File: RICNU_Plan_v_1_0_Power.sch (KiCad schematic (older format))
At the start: 15 parts, among them U1 TPS2113, U2 TLV62568

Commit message: Various small changes like comment removal
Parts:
- R1: value 20k -> 24k
- R5: value 450k -> 453k
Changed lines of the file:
@@
 P 8300 3900
 F 0 "R5" V 8400 3900 50  0000 C CNN
-F 1 "450k" V 8200 3900 50  0000 C CNN
+F 1 "453k" V 8200 3900 50  0000 C CNN
 F 2 "Resistors_SMD:R_0402_NoSilk" V 8230 3900 50  0001 C CNN
 F 3 "" H 8300 3900 50  0001 C CNN
@@
 P 3250 4150
 F 0 "R1" V 3300 3950 50  0000 C CNN
-F 1 "20k" V 3250 4150 50  0000 C CNN
+F 1 "24k" V 3250 4150 50  0000 C CNN
 F 2 "Resistors_SMD:R_0402_NoSilk" V 3180 4150 50  0001 C CNN
 F 3 "" H 3250 4150 50  0001 C CNN
@@
 L PWR_FLAG #FLG06
 U 1 1 5A03C349
-P 4900 5050
-F 0 "#FLG06" H 4900 5125 50  0001 C CNN
-F 1 "PWR_FLAG" H 4900 5200 50  0000 C CNN
-F 2 "" H 4900 5050 50  0001 C CNN
-F 3 "" H 4900 5050 50  0001 C CNN
-	1    4900 5050
+P 4900 5850
+F 0 "#FLG06" H 4900 5925 50  0001 C CNN
+F 1 "PWR_FLAG" H 4900 6000 50  0000 C CNN
+F 2 "" H 4900 5850 50  0001 C CNN
+F 3 "" H 4900 5850 50  0001 C CNN
+	1    4900 5850
 	-1   0    0    1
 $EndComp
@@
 L PWR_FLAG #FLG07
 U 1 1 5A03C34F
-P 4450 4950
-F 0 "#FLG07" H 4450 5025 50  0001 C CNN
-F 1 "PWR_FLAG" H 4450 5100 50  0000 C CNN
-F 2 "" H 4450 4950 50  0001 C CNN
-F 3 "" H 4450 4950 50  0001 C CNN
-	1    4450 4950
+P 4450 5750
+F 0 "#FLG07" H 4450 5825 50  0001 C CNN
+F 1 "PWR_FLAG" H 4450 5900 50  0000 C CNN
+F 2 "" H 4450 5750 50  0001 C CNN
+F 3 "" H 4450 5750 50  0001 C CNN
+	1    4450 5750
 	1    0    0    -1
 $EndComp
@@
 L GND #PWR08
 U 1 1 5A03C355
-P 4450 5050
-F 0 "#PWR08" H 4450 4800 50  0001 C CNN
-F 1 "GND" H 4450 4900 50  0000 C CNN
-F 2 "" H 4450 5050 50  0001 C CNN
-F 3 "" H 4450 5050 50  0001 C CNN
-	1    4450 5050
+P 4450 5850
+F 0 "#PWR08" H 4450 5600 50  0001 C CNN
+F 1 "GND" H 4450 5700 50  0000 C CNN
+F 2 "" H 4450 5850 50  0001 C CNN
+F 3 "" H 4450 5850 50  0001 C CNN
+	1    4450 5850
 	1    0    0    -1
 $EndComp
@@
 L +3V3 #PWR09
 U 1 1 5A03C35B
-P 4900 4950
-F 0 "#PWR09" H 4900 4800 50  0001 C CNN
-F 1 "+3V3" H 4900 5090 50  0000 C CNN
-F 2 "" H 4900 4950 50  0001 C CNN
-F 3 "" H 4900 4950 50  0001 C CNN
-	1    4900 4950
+P 4900 5750
+F 0 "#PWR09" H 4900 5600 50  0001 C CNN
+F 1 "+3V3" H 4900 5890 50  0000 C CNN
+F 2 "" H 4900 5750 50  0001 C CNN
+F 3 "" H 4900 5750 50  0001 C CNN
+	1    4900 5750
 	1    0    0    -1
 $EndComp
@@
 L +5V_USB #PWR010
 U 1 1 5A03C361
-P 5800 4950
-F 0 "#PWR010" H 5800 4800 50  0001 C CNN
-F 1 "+5V_USB" H 5800 5100 50  0000 C CNN
-F 2 "" H 5800 4950 50  0001 C CNN
-F 3 "" H 5800 4950 50  0001 C CNN
-	1    5800 4950
+P 5800 5750
+F 0 "#PWR010" H 5800 5600 50  0001 C CNN
+F 1 "+5V_USB" H 5800 5900 50  0000 C CNN
+F 2 "" H 5800 5750 50  0001 C CNN
+F 3 "" H 5800 5750 50  0001 C CNN
+	1    5800 5750
 	1    0    0    -1
 $EndComp
@@
 L PWR_FLAG #FLG011
 U 1 1 5A03C367
-P 5800 5050
-F 0 "#FLG011" H 5800 5125 50  0001 C CNN
-F 1 "PWR_FLAG" H 5800 5200 50  0000 C CNN
-F 2 "" H 5800 5050 50  0001 C CNN
-F 3 "" H 5800 5050 50  0001 C CNN
-	1    5800 5050
+P 5800 5850
+F 0 "#FLG011" H 5800 5925 50  0001 C CNN
+F 1 "PWR_FLAG" H 5800 6000 50  0000 C CNN
+F 2 "" H 5800 5850 50  0001 C CNN
+F 3 "" H 5800 5850 50  0001 C CNN
+	1    5800 5850
 	-1   0    0    1
 $EndComp
@@
 L +5V_USB_P #PWR012
 U 1 1 5A03C36D
-P 6250 4950
-F 0 "#PWR012" H 6250 4800 50  0001 C CNN
-F 1 "+5V_USB_P" H 6250 5100 50  0000 C CNN
-F 2 "" H 6250 4950 50  0001 C CNN
-F 3 "" H 6250 4950 50  0001 C CNN
-	1    6250 4950
+P 6250 5750
+F 0 "#PWR012" H 6250 5600 50  0001 C CNN
+F 1 "+5V_USB_P" H 6250 5900 50  0000 C CNN
+F 2 "" H 6250 5750 50  0001 C CNN
+F 3 "" H 6250 5750 50  0001 C CNN
+	1    6250 5750
 	1    0    0    -1
 $EndComp
@@
 L PWR_FLAG #FLG013
 U 1 1 5A03C373
-P 6250 5050
-F 0 "#FLG013" H 6250 5125 50  0001 C CNN
-F 1 "PWR_FLAG" H 6250 5200 50  0000 C CNN
-F 2 "" H 6250 5050 50  0001 C CNN
-F 3 "" H 6250 5050 50  0001 C CNN
-	1    6250 5050
+P 6250 5850
+F 0 "#FLG013" H 6250 5925 50  0001 C CNN
+F 1 "PWR_FLAG" H 6250 6000 50  0000 C CNN
+F 2 "" H 6250 5850 50  0001 C CNN
+F 3 "" H 6250 5850 50  0001 C CNN
+	1    6250 5850
 	-1   0    0    1
 $EndComp
@@
 L +5V_EXT #PWR014
 U 1 1 5A03C379
-P 6700 4950
-F 0 "#PWR014" H 6700 4800 50  0001 C CNN
-F 1 "+5V_EXT" H 6700 5100 50  0000 C CNN
-F 2 "" H 6700 4950 50  0001 C CNN
-F 3 "" H 6700 4950 50  0001 C CNN
-	1    6700 4950
+P 6700 5750
+F 0 "#PWR014" H 6700 5600 50  0001 C CNN
+F 1 "+5V_EXT" H 6700 5900 50  0000 C CNN
+F 2 "" H 6700 5750 50  0001 C CNN
+F 3 "" H 6700 5750 50  0001 C CNN
+	1    6700 5750
 	1    0    0    -1
 $EndComp
@@
 L +5V_EXT_P #PWR015
 U 1 1 5A03C37F
-P 7150 4950
-F 0 "#PWR015" H 7150 4800 50  0001 C CNN
-F 1 "+5V_EXT_P" H 7150 5100 50  0000 C CNN
-F 2 "" H 7150 4950 50  0001 C CNN
-F 3 "" H 7150 4950 50  0001 C CNN
-	1    7150 4950
+P 7150 5750
+F 0 "#PWR015" H 7150 5600 50  0001 C CNN
+F 1 "+5V_EXT_P" H 7150 5900 50  0000 C CNN
+F 2 "" H 7150 5750 50  0001 C CNN
+F 3 "" H 7150 5750 50  0001 C CNN
+	1    7150 5750
 	1    0    0    -1
 $EndComp
@@
 L PWR_FLAG #FLG016
 U 1 1 5A03C385
-P 6700 5050
-F 0 "#FLG016" H 6700 5125 50  0001 C CNN
-F 1 "PWR_FLAG" H 6700 5200 50  0000 C CNN
-F 2 "" H 6700 5050 50  0001 C CNN
-F 3 "" H 6700 5050 50  0001 C CNN
-	1    6700 5050
+P 6700 5850
+F 0 "#FLG016" H 6700 5925 50  0001 C CNN
+F 1 "PWR_FLAG" H 6700 6000 50  0000 C CNN
+F 2 "" H 6700 5850 50  0001 C CNN
+F 3 "" H 6700 5850 50  0001 C CNN
+	1    6700 5850
 	-1   0    0    1
 $EndComp
@@
 L PWR_FLAG #FLG017
 U 1 1 5A03C38B
-P 7150 5050
-F 0 "#FLG017" H 7150 5125 50  0001 C CNN
-F 1 "PWR_FLAG" H 7150 5200 50  0000 C CNN
-F 2 "" H 7150 5050 50  0001 C CNN
-F 3 "" H 7150 5050 50  0001 C CNN
-	1    7150 5050
+P 7150 5850
+F 0 "#FLG017" H 7150 5925 50  0001 C CNN
+F 1 "PWR_FLAG" H 7150 6000 50  0000 C CNN
+F 2 "" H 7150 5850 50  0001 C CNN
+F 3 "" H 7150 5850 50  0001 C CNN
+	1    7150 5850
 	-1   0    0    1
 $EndComp
@@
 L +5V #PWR018
 U 1 1 5A03C391
-P 5350 4950
-F 0 "#PWR018" H 5350 4800 50  0001 C CNN
-F 1 "+5V" H 5350 5090 50  0000 C CNN
-F 2 "" H 5350 4950 50  0001 C CNN
-F 3 "" H 5350 4950 50  0001 C CNN
-	1    5350 4950
+P 5350 5750
+F 0 "#PWR018" H 5350 5600 50  0001 C CNN
+F 1 "+5V" H 5350 5890 50  0000 C CNN
+F 2 "" H 5350 5750 50  0001 C CNN
+F 3 "" H 5350 5750 50  0001 C CNN
+	1    5350 5750
 	1    0    0    -1
 $EndComp
@@
 L PWR_FLAG #FLG019
 U 1 1 5A03C397
-P 5350 5050
-F 0 "#FLG019" H 5350 5125 50  0001 C CNN
-F 1 "PWR_FLAG" H 5350 5200 50  0000 C CNN
-F 2 "" H 5350 5050 50  0001 C CNN
-F 3 "" H 5350 5050 50  0001 C CNN
-	1    5350 5050
+P 5350 5850
+F 0 "#FLG019" H 5350 5925 50  0001 C CNN
+F 1 "PWR_FLAG" H 5350 6000 50  0000 C CNN
+F 2 "" H 5350 5850 50  0001 C CNN
+F 3 "" H 5350 5850 50  0001 C CNN
+	1    5350 5850
 	-1   0    0    1
 $EndComp
@@
 Connection ~ 7550 4500
 Wire Wire Line
-	4450 5050 4450 4950
-Wire Wire Line
-	4900 5050 4900 4950
-Wire Wire Line
-	7150 5050 7150 4950
-Wire Wire Line
-	6700 5050 6700 4950
-Wire Wire Line
-	6250 5050 6250 4950
-Wire Wire Line
-	5800 5050 5800 4950
-Wire Wire Line
-	5350 5050 5350 4950
+	4450 5850 4450 5750
+Wire Wire Line
+	4900 5850 4900 5750
+Wire Wire Line
+	7150 5850 7150 5750
+Wire Wire Line
+	6700 5850 6700 5750
+Wire Wire Line
+	6250 5850 6250 5750
+Wire Wire Line
+	5800 5850 5800 5750
+Wire Wire Line
+	5350 5850 5350 5750
 Wire Wire Line
 	8650 3300 8650 3200

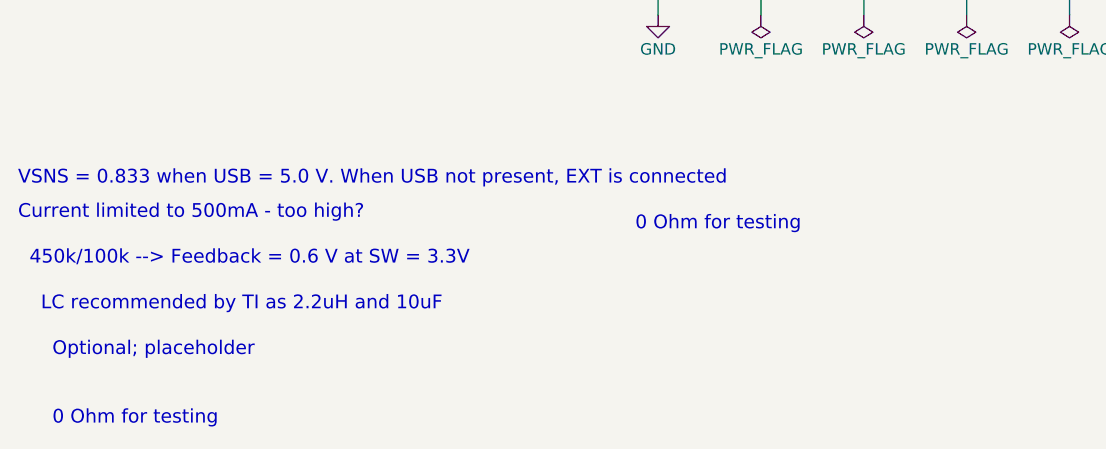
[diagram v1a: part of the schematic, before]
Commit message: Deleting PDFs
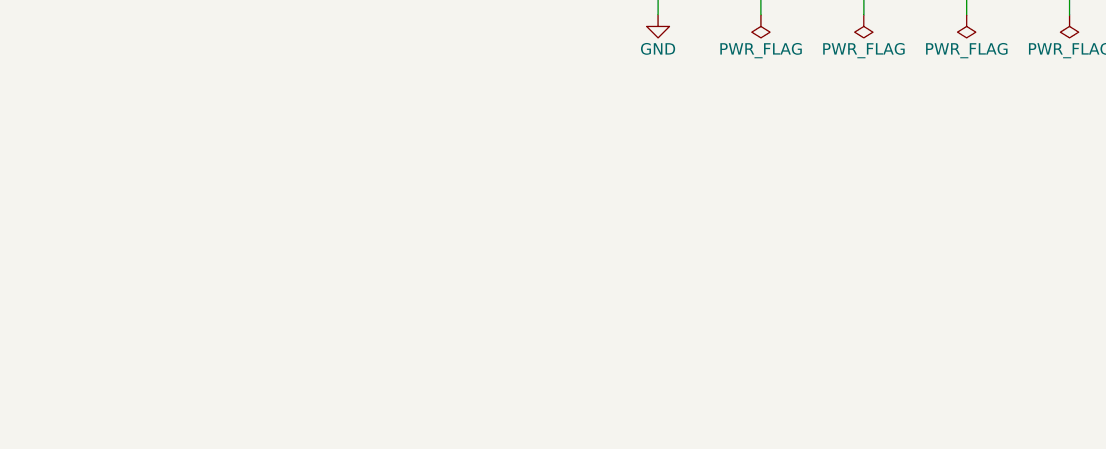
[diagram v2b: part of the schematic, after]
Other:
- note removed: "0 Ohm for testing"
- note removed: "450k/100k --> Feedback = 0.6 V at SW = 3.3V"
- note removed: "Current limited to 500mA - too high?"
- note removed: "LC recommended by TI as 2.2uH and 10uF"
- note removed: "Optional; placeholder"
- note removed: "VSNS = 0.833 when USB = 5.0 V. When USB not present, EXT is connected"
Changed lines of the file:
@@
 	1    0    0    -1
 $EndComp
-Text Notes 4350 6800 0    60   ~ 0
-0 Ohm for testing
-Text Notes 1800 7650 0    60   ~ 0
-0 Ohm for testing
-Text Notes 1700 6950 0    60   ~ 0
-450k/100k --> Feedback = 0.6 V at SW = 3.3V
-Text Notes 1750 7150 0    60   ~ 0
-LC recommended by TI as 2.2uH and 10uF
-Text Notes 1800 7350 0    60   ~ 0
-Optional; placeholder
-Text Notes 1650 6600 0    60   ~ 0
-VSNS = 0.833 when USB = 5.0 V. When USB not present, EXT is connected
-Text Notes 1650 6750 0    60   ~ 0
-Current limited to 500mA - too high?
 $Comp
 L PWR_FLAG #FLG06
